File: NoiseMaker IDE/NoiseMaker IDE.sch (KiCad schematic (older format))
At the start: 17 parts, among them J1 IDE_OUT, J2 IDE_IN, J3 PWR, J4 SPK, M1 Mounting, M2 Mounting, M3 Mounting

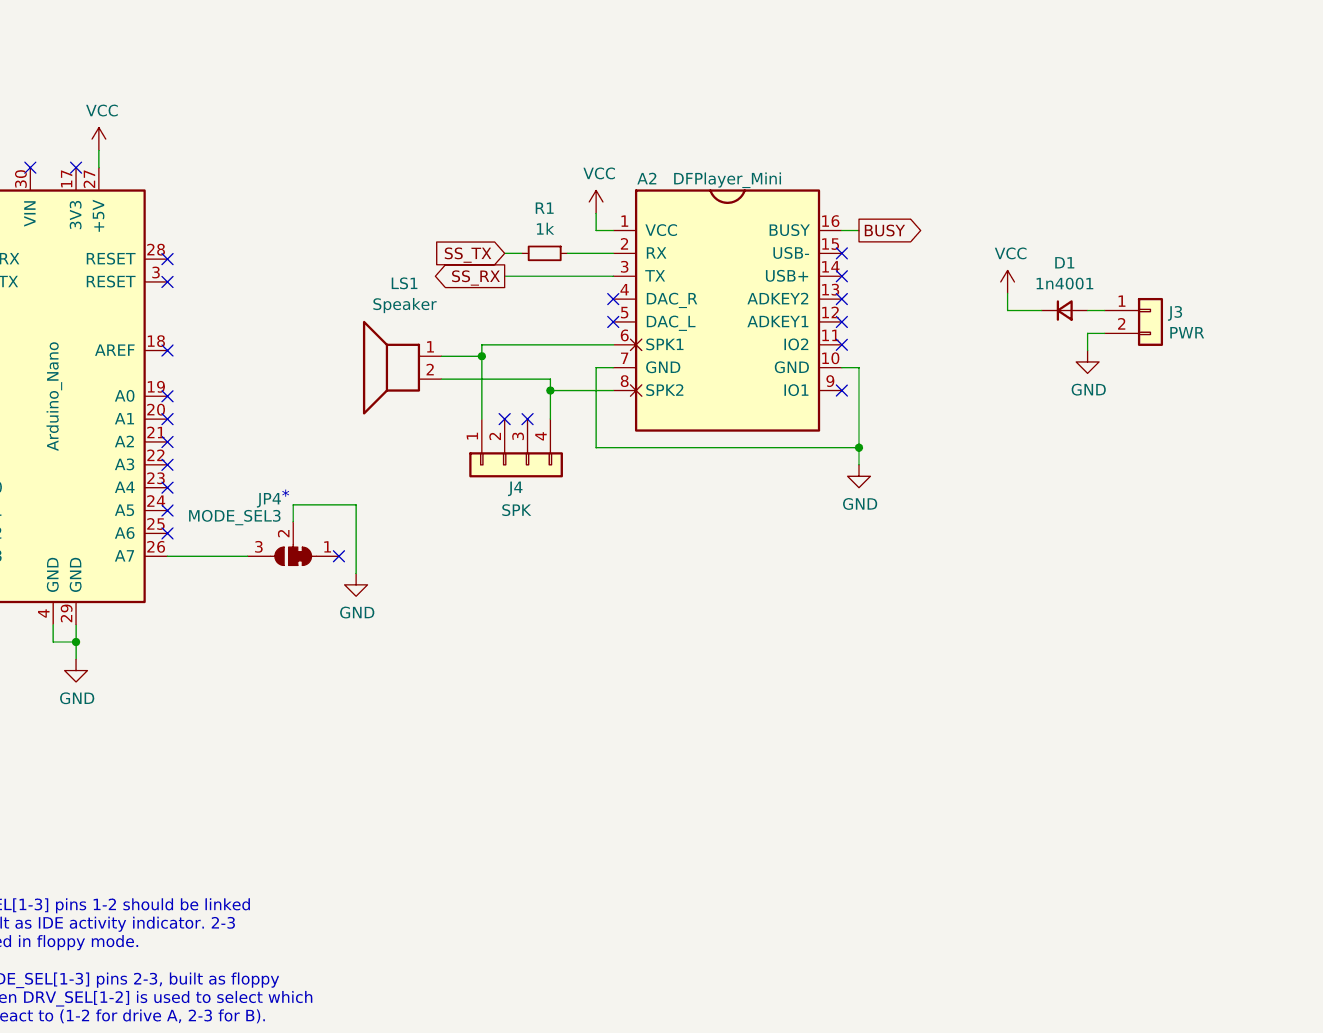
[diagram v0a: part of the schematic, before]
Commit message: Add test button
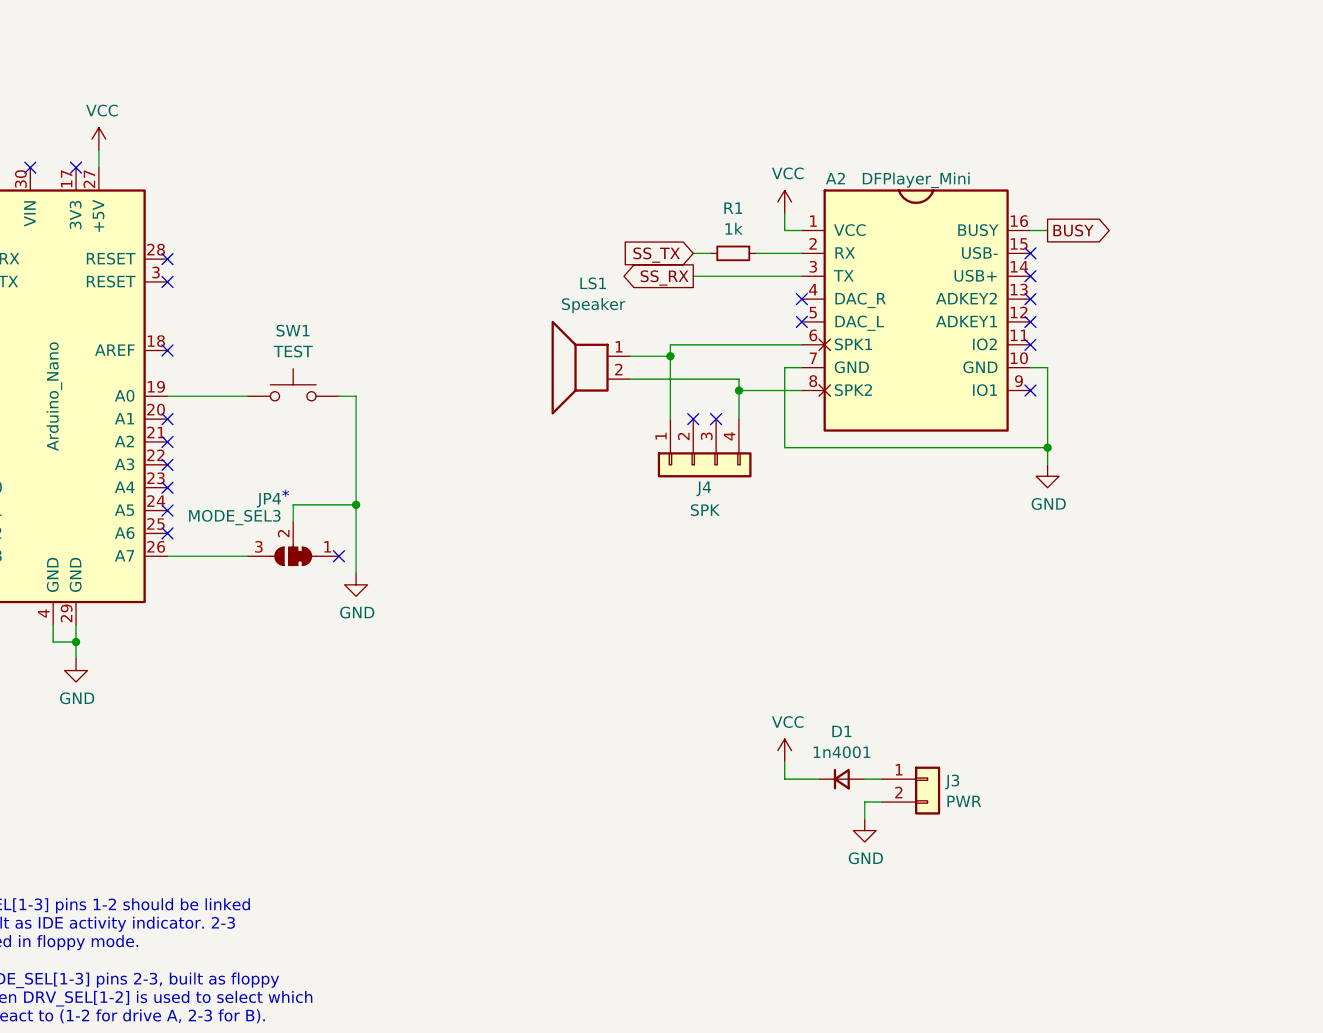
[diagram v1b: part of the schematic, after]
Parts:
- added SW1: TEST, switch_cutout:SW_PUSH_6mm, symbol Switch:SW_Push
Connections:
- net GND: now also SW1.2
- net at A1.19 (A0): now also SW1.1
- no-connect marks 30 -> 29
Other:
- moved on the sheet: A2, D1, J3, J4, LS1, R1
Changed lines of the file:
@@
 L DFPlayer_Mini:DFPlayer_Mini A2
 U 1 1 634CC848
-P 8525 2525
-F 0 "A2" H 8175 2875 50  0000 C CNN
-F 1 "DFPlayer_Mini" H 8525 2875 50  0000 C CNN
-F 2 "DFPlayer_Mini:DFPlayer_Mini" H 8450 2525 50  0001 C CNN
-F 3 "" H 8450 2525 50  0001 C CNN
-	1    8525 2525
-	1    0    0    -1
-$EndComp
-Wire Wire Line
-	8025 3000 7950 3000
-Wire Wire Line
-	7950 3000 7950 3350
-Wire Wire Line
-	7950 3350 9100 3350
-Wire Wire Line
-	9100 3350 9100 3000
-Wire Wire Line
-	9100 3000 9025 3000
-Wire Wire Line
-	9100 3350 9100 3425
-Connection ~ 9100 3350
+P 9350 2525
+F 0 "A2" H 9000 2875 50  0000 C CNN
+F 1 "DFPlayer_Mini" H 9350 2875 50  0000 C CNN
+F 2 "DFPlayer_Mini:DFPlayer_Mini" H 9275 2525 50  0001 C CNN
+F 3 "" H 9275 2525 50  0001 C CNN
+	1    9350 2525
+	1    0    0    -1
+$EndComp
+Wire Wire Line
+	8850 3000 8775 3000
+Wire Wire Line
+	8775 3000 8775 3350
+Wire Wire Line
+	8775 3350 9925 3350
+Wire Wire Line
+	9925 3350 9925 3000
+Wire Wire Line
+	9925 3000 9850 3000
+Wire Wire Line
+	9925 3350 9925 3425
+Connection ~ 9925 3350
 $Comp
 L power:GND #PWR0101
 U 1 1 634CFBE0
-P 9100 3425
-F 0 "#PWR0101" H 9100 3175 50  0001 C CNN
-F 1 "GND" H 9105 3252 50  0000 C CNN
-F 2 "" H 9100 3425 50  0001 C CNN
-F 3 "" H 9100 3425 50  0001 C CNN
-	1    9100 3425
+P 9925 3425
+F 0 "#PWR0101" H 9925 3175 50  0001 C CNN
+F 1 "GND" H 9930 3252 50  0000 C CNN
+F 2 "" H 9925 3425 50  0001 C CNN
+F 3 "" H 9925 3425 50  0001 C CNN
+	1    9925 3425
 	1    0    0    -1
 $EndComp
@@
 L Device:D_Small D1
 U 1 1 634D2772
-P 10000 2750
-F 0 "D1" H 10000 2957 50  0000 C CNN
-F 1 "1n4001" H 10000 2866 50  0000 C CNN
-F 2 "Diode_THT:D_DO-41_SOD81_P12.70mm_Horizontal" V 10000 2750 50  0001 C CNN
-F 3 "~" V 10000 2750 50  0001 C CNN
-	1    10000 2750
+P 9025 4800
+F 0 "D1" H 9025 5007 50  0000 C CNN
+F 1 "1n4001" H 9025 4916 50  0000 C CNN
+F 2 "Diode_THT:D_DO-41_SOD81_P12.70mm_Horizontal" V 9025 4800 50  0001 C CNN
+F 3 "~" V 9025 4800 50  0001 C CNN
+	1    9025 4800
 	1    0    0    -1
 $EndComp
@@
 L Connector_Generic:Conn_01x02 J3
 U 1 1 634D40D7
-P 10375 2750
-F 0 "J3" H 10455 2742 50  0000 L CNN
-F 1 "PWR" H 10455 2651 50  0000 L CNN
-F 2 "noisemaker:Power" H 10375 2750 50  0001 C CNN
-F 3 "~" H 10375 2750 50  0001 C CNN
-	1    10375 2750
+P 9400 4800
+F 0 "J3" H 9480 4792 50  0000 L CNN
+F 1 "PWR" H 9480 4701 50  0000 L CNN
+F 2 "noisemaker:Power" H 9400 4800 50  0001 C CNN
+F 3 "~" H 9400 4800 50  0001 C CNN
+	1    9400 4800
 	1    0    0    -1
 $EndComp
@@
 L power:GND #PWR0102
 U 1 1 634D5854
-P 10100 2925
-F 0 "#PWR0102" H 10100 2675 50  0001 C CNN
-F 1 "GND" H 10105 2752 50  0000 C CNN
-F 2 "" H 10100 2925 50  0001 C CNN
-F 3 "" H 10100 2925 50  0001 C CNN
-	1    10100 2925
-	1    0    0    -1
-$EndComp
-Wire Wire Line
-	10100 2925 10100 2850
-Wire Wire Line
-	10100 2850 10175 2850
-Wire Wire Line
-	10100 2750 10175 2750
+P 9125 4975
+F 0 "#PWR0102" H 9125 4725 50  0001 C CNN
+F 1 "GND" H 9130 4802 50  0000 C CNN
+F 2 "" H 9125 4975 50  0001 C CNN
+F 3 "" H 9125 4975 50  0001 C CNN
+	1    9125 4975
+	1    0    0    -1
+$EndComp
+Wire Wire Line
+	9125 4975 9125 4900
+Wire Wire Line
+	9125 4900 9200 4900
+Wire Wire Line
+	9125 4800 9200 4800
 NoConn ~ 5475 2125
-NoConn ~ 9025 3100
-Wire Wire Line
-	9900 2750 9750 2750
-Wire Wire Line
-	9750 2750 9750 2675
+NoConn ~ 9850 3100
+Wire Wire Line
+	8925 4800 8775 4800
+Wire Wire Line
+	8775 4800 8775 4725
 $Comp
 L power:VCC #PWR03
 U 1 1 634DC01A
-P 9750 2675
-F 0 "#PWR03" H 9750 2525 50  0001 C CNN
-F 1 "VCC" H 9765 2848 50  0000 C CNN
-F 2 "" H 9750 2675 50  0001 C CNN
-F 3 "" H 9750 2675 50  0001 C CNN
-	1    9750 2675
+P 8775 4725
+F 0 "#PWR03" H 8775 4575 50  0001 C CNN
+F 1 "VCC" H 8790 4898 50  0000 C CNN
+F 2 "" H 8775 4725 50  0001 C CNN
+F 3 "" H 8775 4725 50  0001 C CNN
+	1    8775 4725
 	1    0    0    -1
 $EndComp
@@
 	5775 2050 5775 2125
 Wire Wire Line
-	8025 2400 7950 2400
-Wire Wire Line
-	7950 2400 7950 2325
+	8850 2400 8775 2400
+Wire Wire Line
+	8775 2400 8775 2325
 $Comp
 L power:VCC #PWR02
 U 1 1 634DF221
-P 7950 2325
-F 0 "#PWR02" H 7950 2175 50  0001 C CNN
-F 1 "VCC" H 7965 2498 50  0000 C CNN
-F 2 "" H 7950 2325 50  0001 C CNN
-F 3 "" H 7950 2325 50  0001 C CNN
-	1    7950 2325
+P 8775 2325
+F 0 "#PWR02" H 8775 2175 50  0001 C CNN
+F 1 "VCC" H 8790 2498 50  0000 C CNN
+F 2 "" H 8775 2325 50  0001 C CNN
+F 3 "" H 8775 2325 50  0001 C CNN
+	1    8775 2325
 	1    0    0    -1
 $EndComp
@@
 Wire Wire Line
 	5000 3625 5075 3625
-Text GLabel 7550 2500 0    50   Input ~ 0
+Text GLabel 8375 2500 0    50   Input ~ 0
 SS_TX
 $Comp
 L Device:R_Small R1
 U 1 1 634E2B5C
-P 7725 2500
-F 0 "R1" V 7529 2500 50  0000 C CNN
-F 1 "1k" V 7620 2500 50  0000 C CNN
-F 2 "resistor:R_Axial_DIN0207_L6.3mm_D2.5mm_P10.16mm_Horizontal" H 7725 2500 50  0001 C CNN
-F 3 "~" H 7725 2500 50  0001 C CNN
-	1    7725 2500
+P 8550 2500
+F 0 "R1" V 8354 2500 50  0000 C CNN
+F 1 "1k" V 8445 2500 50  0000 C CNN
+F 2 "resistor:R_Axial_DIN0207_L6.3mm_D2.5mm_P10.16mm_Horizontal" H 8550 2500 50  0001 C CNN
+F 3 "~" H 8550 2500 50  0001 C CNN
+	1    8550 2500
 	0    1    1    0
 $EndComp
 Wire Wire Line
-	7550 2500 7625 2500
-Wire Wire Line
-	7825 2500 8025 2500
+	8375 2500 8450 2500
+Wire Wire Line
+	8650 2500 8850 2500
 Text GLabel 5000 3525 0    50   Input ~ 0
 SS_RX
-Text GLabel 7550 2600 0    50   Output ~ 0
+Text GLabel 8375 2600 0    50   Output ~ 0
 SS_RX
 Wire Wire Line
 	5000 3525 5075 3525
 Wire Wire Line
-	7550 2600 8025 2600
+	8375 2600 8850 2600
 $Comp
 L Connector_Generic:Conn_01x04 J4
 U 1 1 634E99A6
-P 7550 3425
-F 0 "J4" V 7650 3375 50  0000 C CNN
-F 1 "SPK" V 7750 3375 50  0000 C CNN
-F 2 "Connector_PinHeader_2.54mm:PinHeader_1x04_P2.54mm_Horizontal" H 7550 3425 50  0001 C CNN
-F 3 "~" H 7550 3425 50  0001 C CNN
-	1    7550 3425
+P 8375 3425
+F 0 "J4" V 8475 3375 50  0000 C CNN
+F 1 "SPK" V 8575 3375 50  0000 C CNN
+F 2 "Connector_PinHeader_2.54mm:PinHeader_1x04_P2.54mm_Horizontal" H 8375 3425 50  0001 C CNN
+F 3 "~" H 8375 3425 50  0001 C CNN
+	1    8375 3425
 	0    -1   1    0
 $EndComp
 Wire Wire Line
-	7450 2950 7275 2950
-Wire Wire Line
-	7450 2950 7450 3225
-Wire Wire Line
-	7450 2950 7450 2900
-Wire Wire Line
-	7450 2900 8025 2900
-Connection ~ 7450 2950
-Wire Wire Line
-	7275 3050 7750 3050
-Wire Wire Line
-	7750 3050 7750 3100
-Wire Wire Line
-	8025 3100 7750 3100
-Connection ~ 7750 3100
-Wire Wire Line
-	7750 3100 7750 3225
-NoConn ~ 7550 3225
-NoConn ~ 7650 3225
+	8275 2950 8100 2950
+Wire Wire Line
+	8275 2950 8275 3225
+Wire Wire Line
+	8275 2950 8275 2900
+Wire Wire Line
+	8275 2900 8850 2900
+Connection ~ 8275 2950
+Wire Wire Line
+	8100 3050 8575 3050
+Wire Wire Line
+	8575 3050 8575 3100
+Wire Wire Line
+	8850 3100 8575 3100
+Connection ~ 8575 3100
+Wire Wire Line
+	8575 3100 8575 3225
+NoConn ~ 8375 3225
+NoConn ~ 8475 3225
 $Comp
 L Device:Speaker LS1
 U 1 1 634E7B91
-P 7075 2950
-F 0 "LS1" H 7038 3267 50  0000 C CNN
-F 1 "Speaker" H 7038 3176 50  0000 C CNN
-F 2 "Buzzer_Beeper:Buzzer_12x9.5RM7.6" H 7075 2750 50  0001 C CNN
-F 3 "~" H 7065 2900 50  0001 C CNN
-	1    7075 2950
+P 7900 2950
+F 0 "LS1" H 7863 3267 50  0000 C CNN
+F 1 "Speaker" H 7863 3176 50  0000 C CNN
+F 2 "Buzzer_Beeper:Buzzer_12x9.5RM7.6" H 7900 2750 50  0001 C CNN
+F 3 "~" H 7890 2900 50  0001 C CNN
+	1    7900 2950
 	-1   0    0    -1
 $EndComp
-NoConn ~ 9025 2900
-NoConn ~ 9025 2800
-NoConn ~ 9025 2700
-NoConn ~ 9025 2600
-NoConn ~ 9025 2500
-Text GLabel 9100 2400 2    50   Output ~ 0
+NoConn ~ 9850 2900
+NoConn ~ 9850 2800
+NoConn ~ 9850 2700
+NoConn ~ 9850 2600
+NoConn ~ 9850 2500
+Text GLabel 9925 2400 2    50   Output ~ 0
 BUSY
 Wire Wire Line
-	9100 2400 9025 2400
+	9925 2400 9850 2400
 Wire Wire Line
 	5675 4125 5675 4200
@@
 NoConn ~ 5075 3325
 NoConn ~ 5075 3425
-NoConn ~ 6075 3125
 NoConn ~ 6075 3225
 NoConn ~ 6075 3325
@@
 NoConn ~ 6075 3625
 NoConn ~ 6075 3725
-NoConn ~ 8025 2700
-NoConn ~ 8025 2800
+NoConn ~ 8850 2700
+NoConn ~ 8850 2800
 $Comp
 L ide_40:IDE J1
@@
 Text Notes 5025 5875 0    50   ~ 0
 With MODE_SEL[1-3] pins 2-3, built as floppy\nmode, then DRV_SEL[1-2] is used to select which\ndrive to react to (1-2 for drive A, 2-3 for B).
+$Comp
+L Switch:SW_Push SW1
+U 1 1 63CE2533
+P 6625 3125
+F 0 "SW1" H 6625 3410 50  0000 C CNN
+F 1 "TEST" H 6625 3319 50  0000 C CNN
+F 2 "switch_cutout:SW_PUSH_6mm" H 6625 3325 50  0001 C CNN
+F 3 "~" H 6625 3325 50  0001 C CNN
+	1    6625 3125
+	1    0    0    -1
+$EndComp
+Wire Wire Line
+	6900 3600 6900 3125
+Wire Wire Line
+	6900 3125 6825 3125
+Connection ~ 6900 3600
+Wire Wire Line
+	6075 3125 6425 3125
 Wire Bus Line
 	1100 2075 1100 7125

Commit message: Tweak silkscreen and dimensions
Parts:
- J1: footprint Connector_PinSocket_2.54mm:PinSocket_2x20_P2.54mm_Vertical -> noisemaker:PinSocket_2x20_P2.54mm_Vertical
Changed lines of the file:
@@
 encoding utf-8
 Sheet 1 1
-Title "NoiseMaker IDE"
+Title "NoiseMaker"
 Date ""
 Rev "A"
@@
 Comment1 ""
 Comment2 ""
-Comment3 ""
-Comment4 "Use with IDE-based storage."
+Comment3 "34-pin floppy alternatives."
+Comment4 "NoiseMaker module for use with 40-pin IDE, alternatively it can be built for use with"
 $EndDescr
 $Comp
@@
 F 0 "J1" H 2025 4542 50  0000 C CNN
 F 1 "IDE_OUT" H 2025 4451 50  0000 C CNN
-F 2 "Connector_PinSocket_2.54mm:PinSocket_2x20_P2.54mm_Vertical" H 2025 3375 50  0001 C CNN
+F 2 "noisemaker:PinSocket_2x20_P2.54mm_Vertical" H 2025 3375 50  0001 C CNN
 F 3 "~" H 2025 3375 50  0001 C CNN
 	1    2025 3375

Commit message: First attempt at sketch
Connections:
- net at A1.24 (A5): now also JP4.3 (B)
- net at A1.26 (A7): no longer JP4.3 (B)
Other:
- moved on the sheet: JP4
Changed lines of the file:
@@
 NoConn ~ 6075 3425
 NoConn ~ 6075 3525
-NoConn ~ 6075 3625
+NoConn ~ 6075 3825
 NoConn ~ 6075 3725
 NoConn ~ 8850 2700
@@
 L power:GND #PWR04
 U 1 1 63AF688F
-P 6900 3900
-F 0 "#PWR04" H 6900 3650 50  0001 C CNN
-F 1 "GND" H 6905 3727 50  0000 C CNN
-F 2 "" H 6900 3900 50  0001 C CNN
-F 3 "" H 6900 3900 50  0001 C CNN
-	1    6900 3900
+P 6900 3700
+F 0 "#PWR04" H 6900 3450 50  0001 C CNN
+F 1 "GND" H 6905 3527 50  0000 C CNN
+F 2 "" H 6900 3700 50  0001 C CNN
+F 3 "" H 6900 3700 50  0001 C CNN
+	1    6900 3700
 	1    0    0    -1
 $EndComp
@@
 L Jumper:SolderJumper_3_Bridged12 JP4
 U 1 1 63BB5A15
-P 6625 3825
-F 0 "JP4" H 6675 3575 50  0000 L CNN
-F 1 "MODE_SEL3" H 6675 3650 50  0000 L CNN
-F 2 "solder_bridge:select2" H 6625 3825 50  0001 C CNN
-F 3 "~" H 6625 3825 50  0001 C CNN
-	1    6625 3825
+P 6625 3625
+F 0 "JP4" H 6675 3375 50  0000 L CNN
+F 1 "MODE_SEL3" H 6675 3450 50  0000 L CNN
+F 2 "solder_bridge:select2" H 6625 3625 50  0001 C CNN
+F 3 "~" H 6625 3625 50  0001 C CNN
+	1    6625 3625
 	-1   0    0    1
 $EndComp
-NoConn ~ 6825 3825
+NoConn ~ 6825 3625
 $Comp
 L Jumper:SolderJumper_3_Bridged12 JP5
@@
 $EndComp
 Wire Wire Line
-	6900 3900 6900 3600
-Wire Wire Line
-	6900 3600 6625 3600
-Wire Wire Line
-	6625 3600 6625 3675
+	6900 3400 6625 3400
+Wire Wire Line
+	6625 3400 6625 3475
 Text Notes 5025 5550 0    50   ~ 0
 MODE_SEL[1-3] pins 1-2 should be linked\nwhen built as IDE activity indicator. 2-3\nwhen used in floppy mode.
 Text Notes 4975 5400 0    50   ~ 0
 *
-Text Notes 6575 3600 0    50   ~ 0
+Text Notes 6575 3400 0    50   ~ 0
 *
 Text Notes 1900 4775 0    50   ~ 0
@@
 *
 Wire Wire Line
-	6075 3825 6425 3825
+	6075 3625 6425 3625
 Text Notes 1850 5875 0    50   ~ 0
 **
@@
 $EndComp
 Wire Wire Line
-	6900 3600 6900 3125
-Wire Wire Line
 	6900 3125 6825 3125
-Connection ~ 6900 3600
 Wire Wire Line
 	6075 3125 6425 3125
+Connection ~ 6900 3400
+Wire Wire Line
+	6900 3400 6900 3125
+Wire Wire Line
+	6900 3400 6900 3700
 Wire Bus Line
 	1100 2075 1100 7125

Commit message: Add proper power connector and more switches
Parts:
- added SW2: VOL_UP, switch_cutout:SW_PUSH_6mm, symbol Switch:SW_Push
- added SW3: VOL_DOWN, switch_cutout:SW_PUSH_6mm, symbol Switch:SW_Push
- J3: footprint noisemaker:Power -> noisemaker:Molex_KK-254_1x04_P2.54mm_Horizontal; symbol Connector_Generic:Conn_01x02 -> Connector_Generic:Conn_01x04
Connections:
- net GND: now also J3.3 (Pin_3), SW2.2, SW3.2
- net at A1.20 (A1): now also SW2.1
- net at A1.21 (A2): now also SW3.1
- net at D1.2 (A): now also J3.4 (Pin_4); no longer J3.1 (Pin_1)
- no-connect marks 29 -> 28
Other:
- moved on the sheet: SW1
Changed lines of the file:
@@
 Title "NoiseMaker"
 Date ""
-Rev "A"
+Rev "B"
 Comp ""
 Comment1 ""
@@
 $EndComp
 $Comp
-L Connector_Generic:Conn_01x02 J3
+L Connector_Generic:Conn_01x04 J3
 U 1 1 634D40D7
-P 9400 4800
-F 0 "J3" H 9480 4792 50  0000 L CNN
-F 1 "PWR" H 9480 4701 50  0000 L CNN
-F 2 "noisemaker:Power" H 9400 4800 50  0001 C CNN
-F 3 "~" H 9400 4800 50  0001 C CNN
-	1    9400 4800
-	1    0    0    -1
+P 9550 5000
+F 0 "J3" H 9630 4992 50  0000 L CNN
+F 1 "PWR" H 9630 4901 50  0000 L CNN
+F 2 "noisemaker:Molex_KK-254_1x04_P2.54mm_Horizontal" H 9550 5000 50  0001 C CNN
+F 3 "~" H 9550 5000 50  0001 C CNN
+	1    9550 5000
+	1    0    0    1
 $EndComp
 $Comp
 L power:GND #PWR0102
 U 1 1 634D5854
-P 9125 4975
-F 0 "#PWR0102" H 9125 4725 50  0001 C CNN
-F 1 "GND" H 9130 4802 50  0000 C CNN
-F 2 "" H 9125 4975 50  0001 C CNN
-F 3 "" H 9125 4975 50  0001 C CNN
-	1    9125 4975
-	1    0    0    -1
-$EndComp
-Wire Wire Line
-	9125 4975 9125 4900
-Wire Wire Line
-	9125 4900 9200 4900
-Wire Wire Line
-	9125 4800 9200 4800
+P 9250 5175
+F 0 "#PWR0102" H 9250 4925 50  0001 C CNN
+F 1 "GND" H 9255 5002 50  0000 C CNN
+F 2 "" H 9250 5175 50  0001 C CNN
+F 3 "" H 9250 5175 50  0001 C CNN
+	1    9250 5175
+	1    0    0    -1
+$EndComp
 NoConn ~ 5475 2125
 NoConn ~ 9850 3100
@@
 NoConn ~ 5075 3325
 NoConn ~ 5075 3425
-NoConn ~ 6075 3225
-NoConn ~ 6075 3325
 NoConn ~ 6075 3425
 NoConn ~ 6075 3525
@@
 L Switch:SW_Push SW1
 U 1 1 63CE2533
+P 6625 2425
+F 0 "SW1" H 6625 2675 50  0000 C CNN
+F 1 "TEST" H 6625 2600 50  0000 C CNN
+F 2 "switch_cutout:SW_PUSH_6mm" H 6625 2625 50  0001 C CNN
+F 3 "~" H 6625 2625 50  0001 C CNN
+	1    6625 2425
+	1    0    0    -1
+$EndComp
+Wire Wire Line
+	6900 2775 6825 2775
+Connection ~ 6900 3400
+Wire Wire Line
+	6900 3400 6900 3700
+Wire Wire Line
+	9350 4900 9250 4900
+Wire Wire Line
+	9350 5000 9250 5000
+Wire Wire Line
+	9250 5000 9250 4900
+Wire Wire Line
+	9250 5000 9250 5175
+Connection ~ 9250 5000
+NoConn ~ 9350 5100
+Wire Wire Line
+	9125 4800 9350 4800
+$Comp
+L Switch:SW_Push SW2
+U 1 1 637DB949
+P 6625 2775
+F 0 "SW2" H 6625 3025 50  0000 C CNN
+F 1 "VOL_UP" H 6625 2950 50  0000 C CNN
+F 2 "switch_cutout:SW_PUSH_6mm" H 6625 2975 50  0001 C CNN
+F 3 "~" H 6625 2975 50  0001 C CNN
+	1    6625 2775
+	1    0    0    -1
+$EndComp
+$Comp
+L Switch:SW_Push SW3
+U 1 1 637E8C02
 P 6625 3125
-F 0 "SW1" H 6625 3410 50  0000 C CNN
-F 1 "TEST" H 6625 3319 50  0000 C CNN
+F 0 "SW3" H 6625 3375 50  0000 C CNN
+F 1 "VOL_DOWN" H 6625 3300 50  0000 C CNN
 F 2 "switch_cutout:SW_PUSH_6mm" H 6625 3325 50  0001 C CNN
 F 3 "~" H 6625 3325 50  0001 C CNN
@@
 $EndComp
 Wire Wire Line
-	6900 3125 6825 3125
-Wire Wire Line
-	6075 3125 6425 3125
-Connection ~ 6900 3400
-Wire Wire Line
-	6900 3400 6900 3125
-Wire Wire Line
-	6900 3400 6900 3700
+	6900 2775 6900 3125
+Wire Wire Line
+	6900 2775 6900 2425
+Wire Wire Line
+	6900 2425 6825 2425
+Connection ~ 6900 2775
+Wire Wire Line
+	6425 2425 6150 2425
+Wire Wire Line
+	6150 2425 6150 3125
+Wire Wire Line
+	6150 3125 6075 3125
+Wire Wire Line
+	6250 3225 6250 2775
+Wire Wire Line
+	6250 2775 6425 2775
+Wire Wire Line
+	6075 3225 6250 3225
+Wire Wire Line
+	6350 3125 6425 3125
+Wire Wire Line
+	6350 3125 6350 3325
+Wire Wire Line
+	6075 3325 6350 3325
+Wire Wire Line
+	6825 3125 6900 3125
 Wire Bus Line
 	1100 2075 1100 7125
@@
 Wire Bus Line
 	1400 2075 1400 4225
+Connection ~ 6900 3125
+Wire Wire Line
+	6900 3125 6900 3400
 $EndSCHEMATC
